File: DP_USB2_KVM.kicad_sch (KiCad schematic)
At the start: 145 parts, among them SW4.KVM? 1-1825027-1

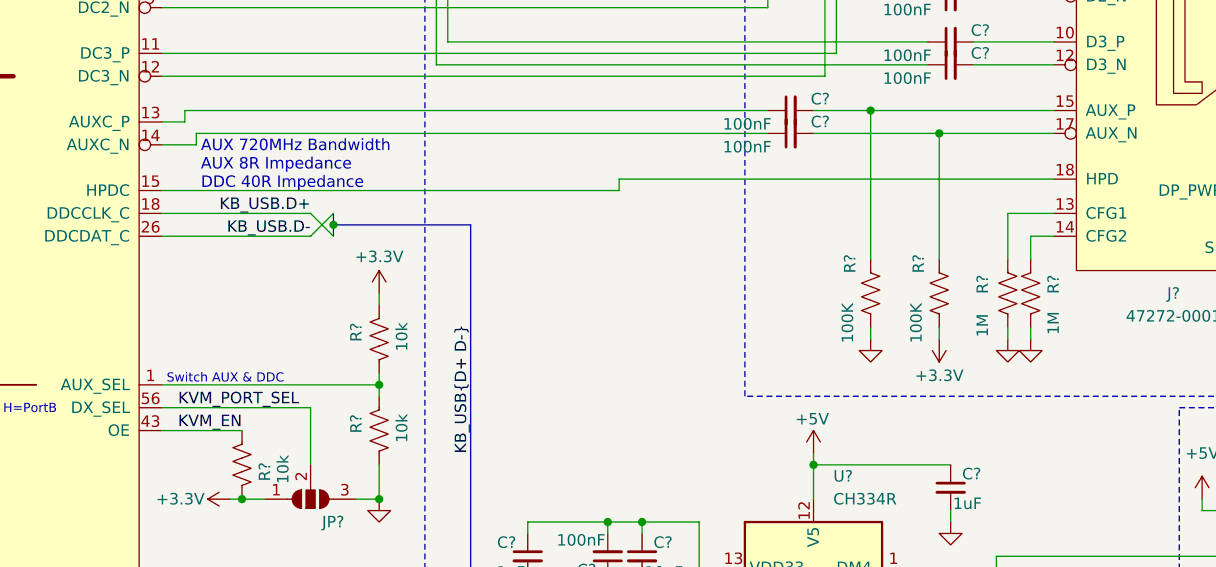
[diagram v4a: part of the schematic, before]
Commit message: BUG Fix: DisplayPort HPD needs a pull b/c Monitor will pull it down when connected.
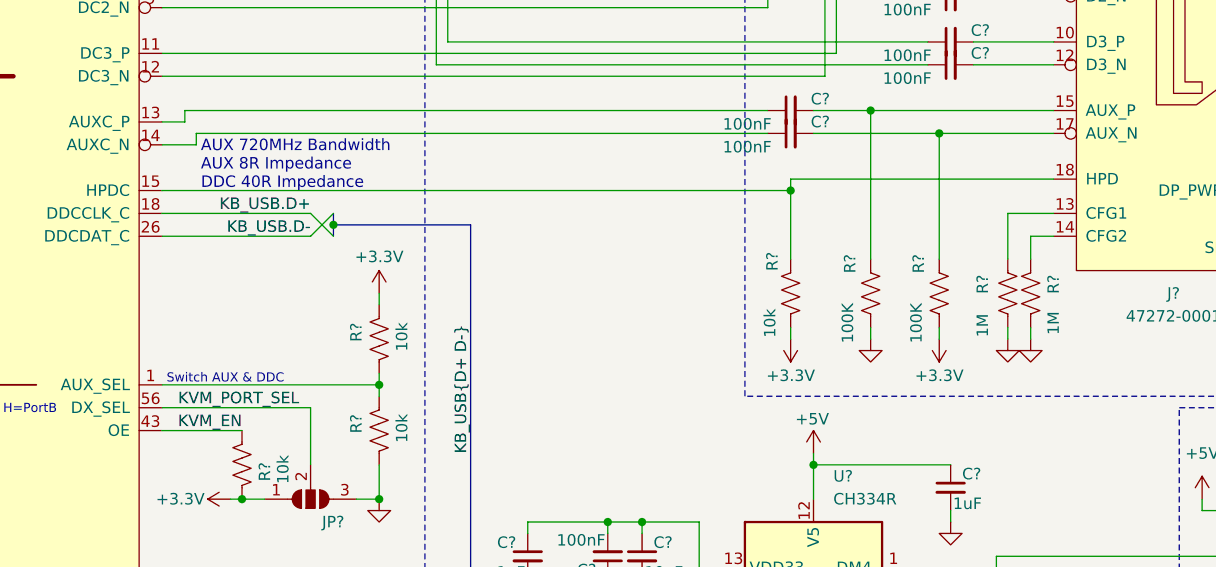
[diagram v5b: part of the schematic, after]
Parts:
- added R?: 10k, Resistor_SMD:R_0603_1608Metric_Pad0.98x0.95mm_HandSolder, symbol Device:R_US
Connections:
- net +3.3V: now also R?.1
- net at J?.18 (HPD), U?.15 (HPDC): now also R?.2
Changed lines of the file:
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@@
 	)
 	(junction
+		(at 426.72 152.4)
+		(diameter 0)
+		(color 0 0 0 0)
+	)
+	(junction
 		(at 80.01 69.85)
 		(diameter 0)
@@
 	(wire
 		(pts
+			(xy 426.72 152.4) (xy 426.72 160.02)
+		)
+		(stroke
+			(width 0)
+			(type default)
+		)
+	)
+	(wire
+		(pts
 			(xy 236.22 80.01) (xy 236.22 77.47)
 		)
@@
 	(wire
 		(pts
-			(xy 407.67 152.4) (xy 356.87 152.4)
+			(xy 426.72 152.4) (xy 356.87 152.4)
 		)
 		(stroke
@@
 	(wire
 		(pts
+			(xy 426.72 167.64) (xy 426.72 168.91)
+		)
+		(stroke
+			(width 0)
+			(type default)
+		)
+	)
+	(wire
+		(pts
 			(xy 447.04 130.81) (xy 455.93 130.81)
 		)
@@
 	(wire
 		(pts
-			(xy 407.67 151.13) (xy 407.67 152.4)
+			(xy 426.72 151.13) (xy 426.72 152.4)
 		)
 		(stroke
@@
 	(wire
 		(pts
-			(xy 455.93 151.13) (xy 407.67 151.13)
+			(xy 455.93 151.13) (xy 426.72 151.13)
 		)
 		(stroke
@@
 	)
 	(symbol
+		(lib_id "power:+3.3V")
+		(at 426.72 168.91 180)
+		(unit 1)
+		(exclude_from_sim no)
+		(in_bom yes)
+		(on_board yes)
+		(dnp no)
+		(property "Reference" "#PWR?"
+			(at 426.72 165.1 0)
+			(effects
+				(font
+					(size 1.27 1.27)
+				)
+				(hide yes)
+			)
+		)
+		(property "Value" "+3.3V"
+			(at 426.72 172.974 0)
+			(effects
+				(font
+					(size 1.27 1.27)
+				)
+			)
+		)
+		(property "Footprint" ""
+			(at 426.72 168.91 0)
+			(effects
+				(font
+					(size 1.27 1.27)
+				)
+				(hide yes)
+			)
+		)
+		(property "Datasheet" ""
+			(at 426.72 168.91 0)
+			(effects
+				(font
+					(size 1.27 1.27)
+				)
+				(hide yes)
+			)
+		)
+		(property "Description" "Power symbol creates a global label with name \"+3.3V\""
+			(at 426.72 168.91 0)
+			(effects
+				(font
+					(size 1.27 1.27)
+				)
+				(hide yes)
+			)
+		)
+		(pin "1"
+		)
+		(instances
+			(project "b1200"
+				(path "/0b04800c-ea22-4b39-b754-6bceaeb1d8a1/9a54e776-69b7-4368-a2d9-dd84cdb57989"
+					(reference "#PWR?")
+					(unit 1)
+				)
+			)
+		)
+	)
+	(symbol
 		(lib_id "Jumper:SolderJumper_2_Open")
 		(at 88.9 363.22 180)
@@
 					(unit 1)
 				)
+			)
+		)
+	)
+	(symbol
+		(lib_id "Device:R_US")
+		(at 426.72 163.83 0)
+		(mirror x)
+		(unit 1)
+		(exclude_from_sim no)
+		(in_bom yes)
+		(on_board yes)
+		(dnp no)
+		(property "Reference" "R?"
+			(at 424.688 160.274 90)
+			(effects
+				(font
+					(size 1.27 1.27)
+				)
+			)
+		)
+		(property "Value" "10k"
+			(at 424.434 167.132 90)
+			(effects
+				(font
+					(size 1.27 1.27)
+				)
+			)
+		)
+		(property "Footprint" "Resistor_SMD:R_0603_1608Metric_Pad0.98x0.95mm_HandSolder"
+			(at 427.736 163.576 90)
+			(effects
+				(font
+					(size 1.27 1.27)
+				)
+				(hide yes)
+			)
+		)
+		(property "Datasheet" "~"
+			(at 426.72 163.83 0)
+			(effects
+				(font
+					(size 1.27 1.27)
+				)
+				(hide yes)
+			)
+		)
+		(property "Description" "Resistor, US symbol"
+			(at 426.72 163.83 0)
+			(effects
+				(font
+					(size 1.27 1.27)
+				)
+				(hide yes)
+			)
+		)
+		(property "Arrow Part Number" ""
+			(at 426.72 163.83 0)
+			(effects
+				(font
+					(size 1.27 1.27)
+				)
+				(hide yes)
+			)
+		)
+		(property "Arrow Price/Stock" ""
+			(at 426.72 163.83 0)
+			(effects
+				(font
+					(size 1.27 1.27)
+				)
+				(hide yes)
+			)
+		)
+		(property "Height" ""
+			(at 426.72 163.83 0)
+			(effects
+				(font
+					(size 1.27 1.27)
+				)
+				(hide yes)
+			)
+		)
+		(property "Manufacturer_Name" ""
+			(at 426.72 163.83 0)
+			(effects
+				(font
+					(size 1.27 1.27)
+				)
+				(hide yes)
+			)
+		)
+		(property "Manufacturer_Part_Number" ""
+			(at 426.72 163.83 0)
+			(effects
+				(font
+					(size 1.27 1.27)
+				)
+				(hide yes)
+			)
+		)
+		(property "Mouser Part Number" ""
+			(at 426.72 163.83 0)
+			(effects
+				(font
+					(size 1.27 1.27)
+				)
+				(hide yes)
+			)
+		)
+		(property "Mouser Price/Stock" ""
+			(at 426.72 163.83 0)
+			(effects
+				(font
+					(size 1.27 1.27)
+				)
+				(hide yes)
+			)
+		)
+		(pin "2"
+		)
+		(pin "1"
+		)
+		(instances
+			(project "b1200"
+				(path "/0b04800c-ea22-4b39-b754-6bceaeb1d8a1/9a54e776-69b7-4368-a2d9-dd84cdb57989"
+					(reference "R?")
+					(unit 1)
+				)
